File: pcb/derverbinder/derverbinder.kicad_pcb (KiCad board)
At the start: 2 copper layers, 2 parts

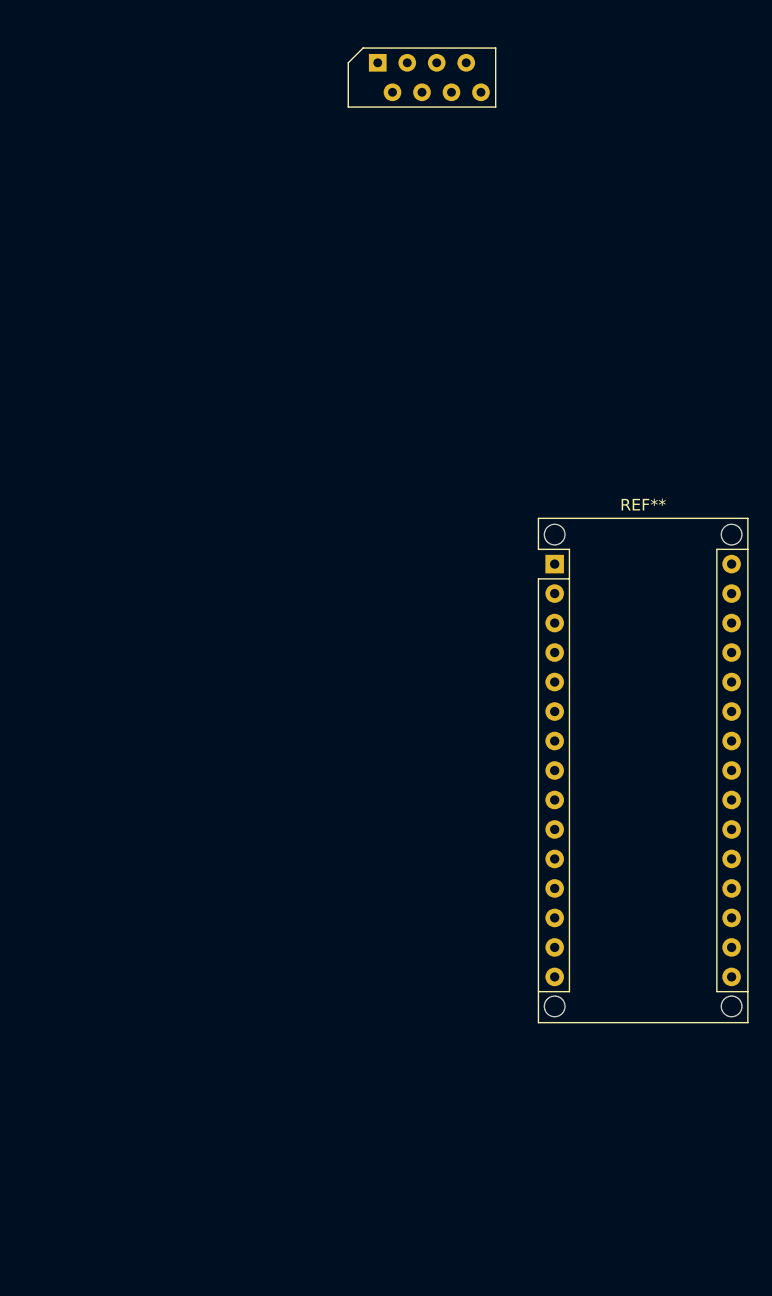
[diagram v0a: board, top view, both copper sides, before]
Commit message: PCB-Routing gemacht, PCB und Schema stimmen NICHT überein
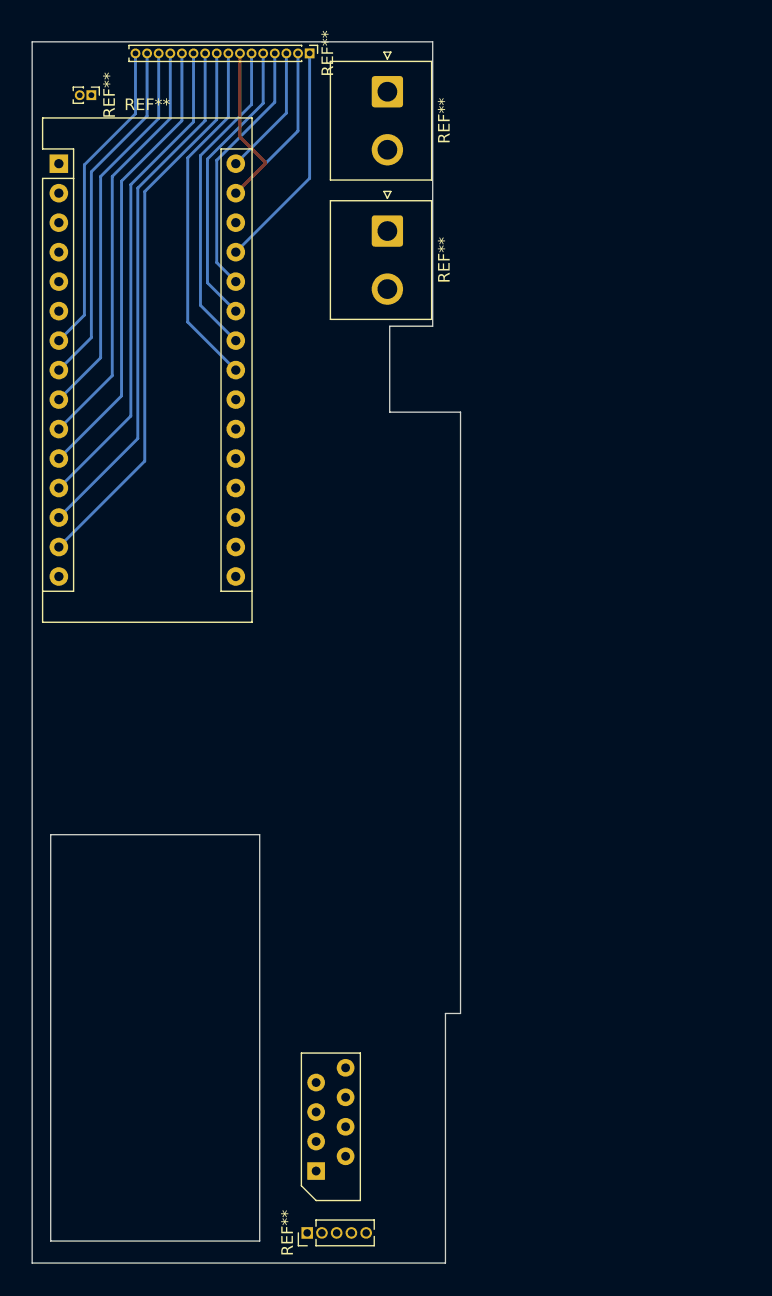
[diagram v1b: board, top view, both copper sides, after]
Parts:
- removed the REF** at (118.1, 110.5)
- added REF**: Arduino_Nano, Module:Arduino_Nano, F.Cu at (75.4, 76.0)
- added REF**: JST_NV_B02P-NV_1x02_P5.00mm_Vertical, Connector_JST:JST_NV_B02P-NV_1x02_P5.00mm_Vertical, F.Cu at (103.7, 81.8)
- added REF**: JST_NV_B02P-NV_1x02_P5.00mm_Vertical, Connector_JST:JST_NV_B02P-NV_1x02_P5.00mm_Vertical, F.Cu at (103.7, 69.8)
- added REF**: PinHeader_1x16_P1.00mm_Vertical, Connector_PinHeader_1.00mm:PinHeader_1x16_P1.00mm_Vertical, F.Cu at (97.0, 66.5)
- added REF**: PinHeader_1x02_P1.00mm_Vertical, Connector_PinHeader_1.00mm:PinHeader_1x02_P1.00mm_Vertical, F.Cu at (78.2, 70.1)
- added REF**: PinHeader_1x05_P1.27mm_Vertical, Connector_PinHeader_1.27mm:PinHeader_1x05_P1.27mm_Vertical, F.Cu at (96.8, 168.1)
- moved REF** 92.4 mm to (96.3, 157.7), turned to 90 degrees
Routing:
- net (no net): track 0.00 -> 467.7 mm
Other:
- board outline added: 36.9 x 105.2 mm
- net class Default: clearance 0.2 -> 0.1
- rule trace_clearance: 0.2 -> 0.1

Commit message: Rerouting
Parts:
- added REF**: TestPoint_Pad_4.0x4.0mm, TestPoint:TestPoint_Pad_4.0x4.0mm, F.Cu at (85.3, 122.0)
- added REF**: TestPoint_Pad_4.0x4.0mm, TestPoint:TestPoint_Pad_4.0x4.0mm, F.Cu at (79.4, 122.0)
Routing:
- net (no net): track 467.7 -> 563.6 mm
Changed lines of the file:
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@@
     (thickness 1.6)
     (drawings 21)
-    (tracks 58)
+    (tracks 63)
     (zones 0)
-    (modules 7)
+    (modules 9)
     (nets 1)
   )
@@
     (mod_text_size 1 1)
     (mod_text_width 0.15)
-    (pad_size 1.524 1.524)
-    (pad_drill 0.762)
+    (pad_size 4 4)
+    (pad_drill 0)
     (pad_to_mask_clearance 0.051)
     (solder_mask_min_width 0.25)
@@
     (uvia_dia 0.3)
     (uvia_drill 0.1)
+  )
+  (module TestPoint:TestPoint_Pad_4.0x4.0mm (layer F.Cu)
+    (at 85.3 122)
+    (descr "SMD rectangular pad as test Point, square 4.0mm side length")
+    (tags "test point SMD pad rectangle square")
+    (attr virtual)
+    (fp_text reference REF** (at 0 -2.898) (layer F.SilkS)
+      (effects (font (size 1 1) (thickness 0.15)))
+    )
+    (fp_text value TestPoint_Pad_4.0x4.0mm (at 0 3.1) (layer F.Fab)
+      (effects (font (size 1 1) (thickness 0.15)))
+    )
+    (fp_text user %R (at 0 -2.9) (layer F.Fab)
+      (effects (font (size 1 1) (thickness 0.15)))
+    )
+    (fp_line (start -2.2 -2.2) (end 2.2 -2.2) (layer F.SilkS) (width 0.12))
+    (fp_line (start 2.2 -2.2) (end 2.2 2.2) (layer F.SilkS) (width 0.12))
+    (fp_line (start 2.2 2.2) (end -2.2 2.2) (layer F.SilkS) (width 0.12))
+    (fp_line (start -2.2 2.2) (end -2.2 -2.2) (layer F.SilkS) (width 0.12))
+    (fp_line (start -2.5 -2.5) (end 2.5 -2.5) (layer F.CrtYd) (width 0.05))
+    (fp_line (start -2.5 -2.5) (end -2.5 2.5) (layer F.CrtYd) (width 0.05))
+    (fp_line (start 2.5 2.5) (end 2.5 -2.5) (layer F.CrtYd) (width 0.05))
+    (fp_line (start 2.5 2.5) (end -2.5 2.5) (layer F.CrtYd) (width 0.05))
+    (pad + connect rect (at 0 0) (size 4 4) (layers F.Cu F.Mask))
+  )
+  (module TestPoint:TestPoint_Pad_4.0x4.0mm (layer F.Cu)
+    (at 79.4 122)
+    (descr "SMD rectangular pad as test Point, square 4.0mm side length")
+    (tags "test point SMD pad rectangle square")
+    (attr virtual)
+    (fp_text reference REF** (at 0 -2.898) (layer F.SilkS)
+      (effects (font (size 1 1) (thickness 0.15)))
+    )
+    (fp_text value TestPoint_Pad_4.0x4.0mm (at 0 3.1) (layer F.Fab)
+      (effects (font (size 1 1) (thickness 0.15)))
+    )
+    (fp_text user %R (at 0 -2.9) (layer F.Fab)
+      (effects (font (size 1 1) (thickness 0.15)))
+    )
+    (fp_line (start -2.2 -2.2) (end 2.2 -2.2) (layer F.SilkS) (width 0.12))
+    (fp_line (start 2.2 -2.2) (end 2.2 2.2) (layer F.SilkS) (width 0.12))
+    (fp_line (start 2.2 2.2) (end -2.2 2.2) (layer F.SilkS) (width 0.12))
+    (fp_line (start -2.2 2.2) (end -2.2 -2.2) (layer F.SilkS) (width 0.12))
+    (fp_line (start -2.5 -2.5) (end 2.5 -2.5) (layer F.CrtYd) (width 0.05))
+    (fp_line (start -2.5 -2.5) (end -2.5 2.5) (layer F.CrtYd) (width 0.05))
+    (fp_line (start 2.5 2.5) (end 2.5 -2.5) (layer F.CrtYd) (width 0.05))
+    (fp_line (start 2.5 2.5) (end -2.5 2.5) (layer F.CrtYd) (width 0.05))
+    (pad - smd rect (at 0 0) (size 4 4) (layers F.Cu F.Mask))
   )
   (module Module:Arduino_Nano (layer F.Cu)
@@
   (segment (start 86.5 75.5) (end 86.5 89.64) (width 0.25) (layer B.Cu) (net 0))
   (segment (start 90 72) (end 86.5 75.5) (width 0.25) (layer B.Cu) (net 0))
+  (segment (start 90.64 78.54) (end 84.96 78.54) (width 0.25) (layer F.Cu) (net 0))
+  (segment (start 84.96 78.54) (end 80.7 82.8) (width 0.25) (layer F.Cu) (net 0))
+  (segment (start 80.7 82.8) (end 80.7 122) (width 0.25) (layer F.Cu) (net 0))
+  (segment (start 90.64 83.62) (end 84.1 83.62) (width 0.25) (layer F.Cu) (net 0))
+  (segment (start 84.1 83.62) (end 84.1 122.1) (width 0.25) (layer F.Cu) (net 0))
 )

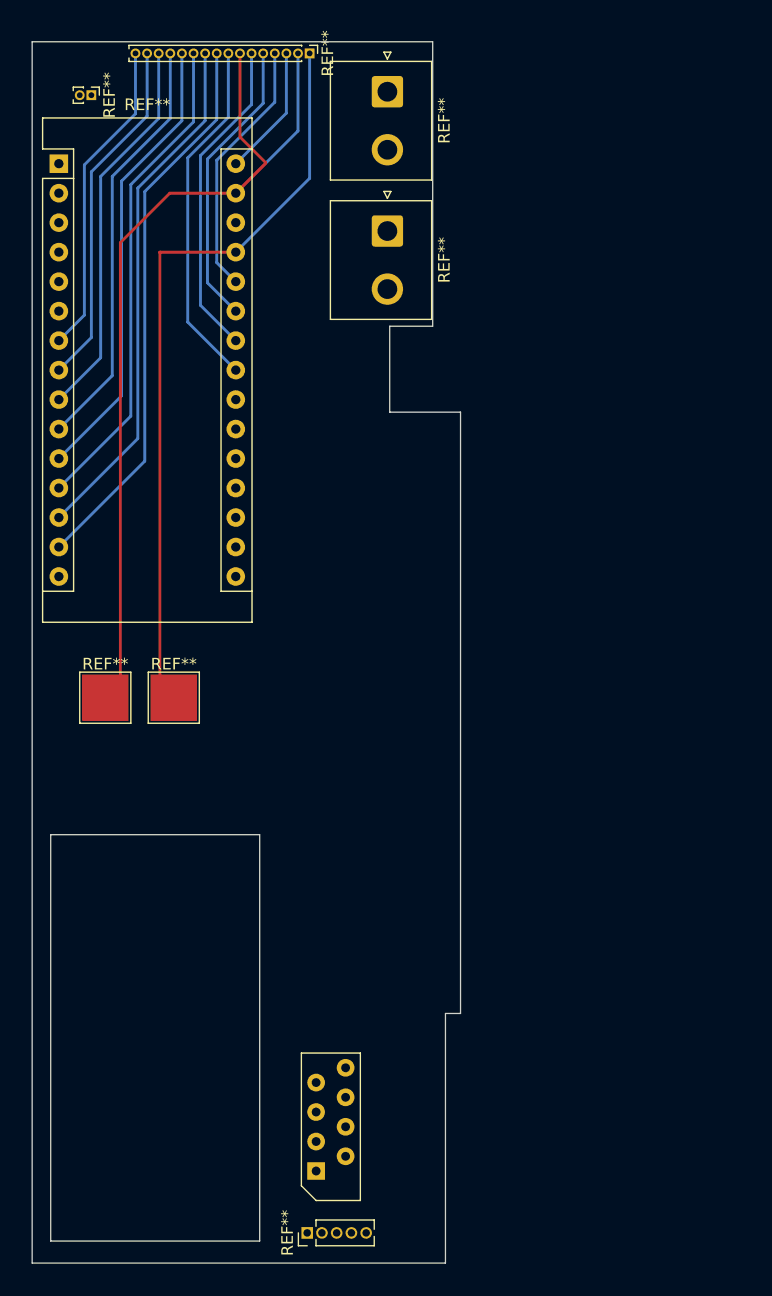
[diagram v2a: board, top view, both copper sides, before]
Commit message: Rerouting
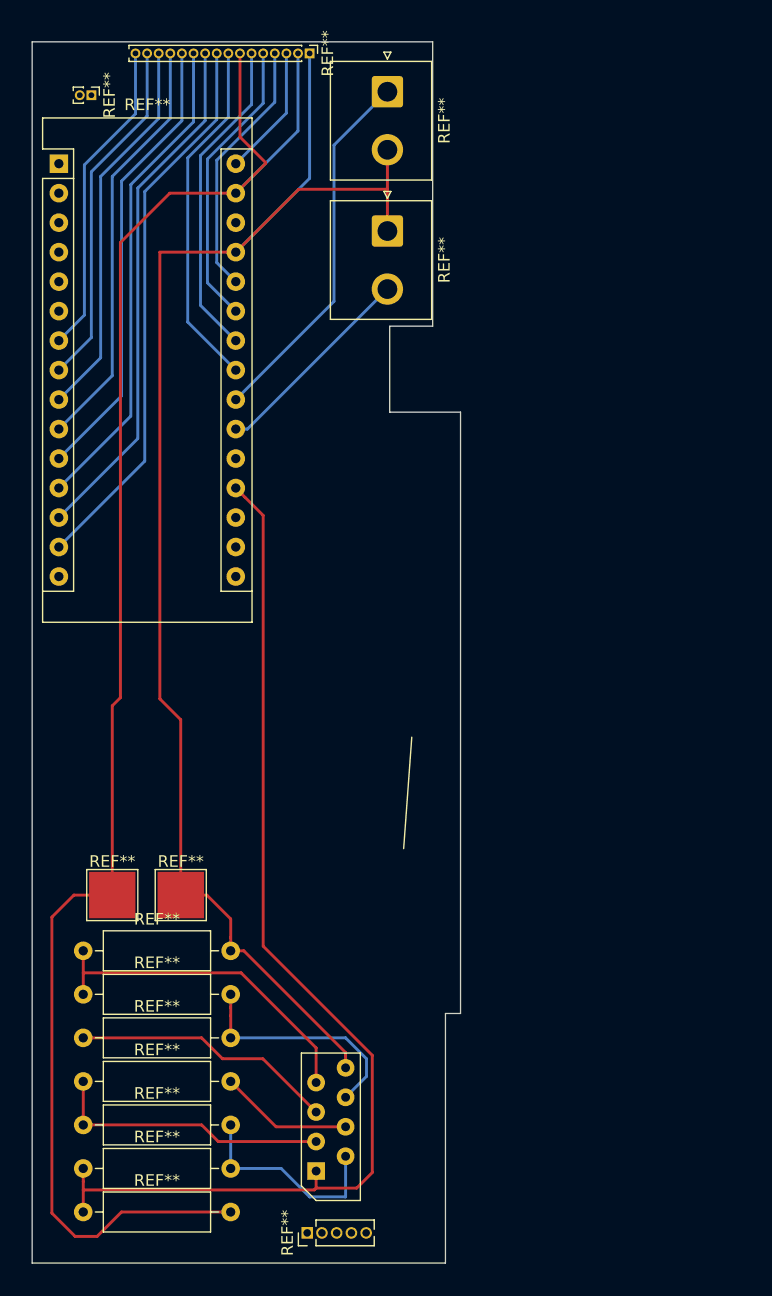
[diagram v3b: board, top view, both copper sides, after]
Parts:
- removed the REF** at (85.3, 122.0)
- removed the REF** at (79.4, 122.0)
- added REF**: R_Axial_DIN0309_L9.0mm_D3.2mm_P12.70mm_Horizontal, Resistor_THT:R_Axial_DIN0309_L9.0mm_D3.2mm_P12.70mm_Horizontal, F.Cu at (77.5, 166.3)
- added REF**: R_Axial_DIN0309_L9.0mm_D3.2mm_P12.70mm_Horizontal, Resistor_THT:R_Axial_DIN0309_L9.0mm_D3.2mm_P12.70mm_Horizontal, F.Cu at (77.5, 162.6)
- added REF**: R_Axial_DIN0309_L9.0mm_D3.2mm_P12.70mm_Horizontal, Resistor_THT:R_Axial_DIN0309_L9.0mm_D3.2mm_P12.70mm_Horizontal, F.Cu at (77.5, 158.8)
- added REF**: R_Axial_DIN0309_L9.0mm_D3.2mm_P12.70mm_Horizontal, Resistor_THT:R_Axial_DIN0309_L9.0mm_D3.2mm_P12.70mm_Horizontal, F.Cu at (77.5, 155.1)
- added REF**: R_Axial_DIN0309_L9.0mm_D3.2mm_P12.70mm_Horizontal, Resistor_THT:R_Axial_DIN0309_L9.0mm_D3.2mm_P12.70mm_Horizontal, F.Cu at (77.5, 151.3)
- added REF**: R_Axial_DIN0309_L9.0mm_D3.2mm_P12.70mm_Horizontal, Resistor_THT:R_Axial_DIN0309_L9.0mm_D3.2mm_P12.70mm_Horizontal, F.Cu at (77.5, 147.6)
- added REF**: R_Axial_DIN0309_L9.0mm_D3.2mm_P12.70mm_Horizontal, Resistor_THT:R_Axial_DIN0309_L9.0mm_D3.2mm_P12.70mm_Horizontal, F.Cu at (77.5, 143.8)
- added REF**: TestPoint_Pad_4.0x4.0mm, TestPoint:TestPoint_Pad_4.0x4.0mm, F.Cu at (85.9, 139.0)
- added REF**: TestPoint_Pad_4.0x4.0mm, TestPoint:TestPoint_Pad_4.0x4.0mm, F.Cu at (80.0, 139.0)
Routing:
- net (no net): track 563.6 -> 963.3 mm
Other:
- outline, holes or cut-outs redrawn

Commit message: PCB finalisiert
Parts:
- added REF**: PinHeader_1x03_P2.00mm_Vertical, Connector_PinHeader_2.00mm:PinHeader_1x03_P2.00mm_Vertical, F.Cu at (74.9, 138.4)
- added REF**: Stocko_MKS_1654-6-0-404_1x4_P2.50mm_Vertical, Connector_Stocko:Stocko_MKS_1654-6-0-404_1x4_P2.50mm_Vertical, F.Cu at (99.1, 130.8)
- moved REF** 0.81 mm to (96.8, 168.9)
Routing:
- net (no net): track 963.3 -> 1187.5 mm
